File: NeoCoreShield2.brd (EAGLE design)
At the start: 70.9 x 70.4 mm, 41 parts, among them J6 BINDER_M12_PAR_8_DIP, J7 BINDER_M12_PAR_8_DIP, J8 BINDER_M12_PAR_8_DIP, J9 BINDER_M12_PAR_8_DIP, Q1 2.5A/30V/105mΩ, Q2 310mA/60V/1.6Ω, Q3 2.5A/30V/105mΩ, Q4 2.5A/30V/105mΩ, Q5 310mA/60V/1.6Ω, Q6 310mA/60V/1.6Ω

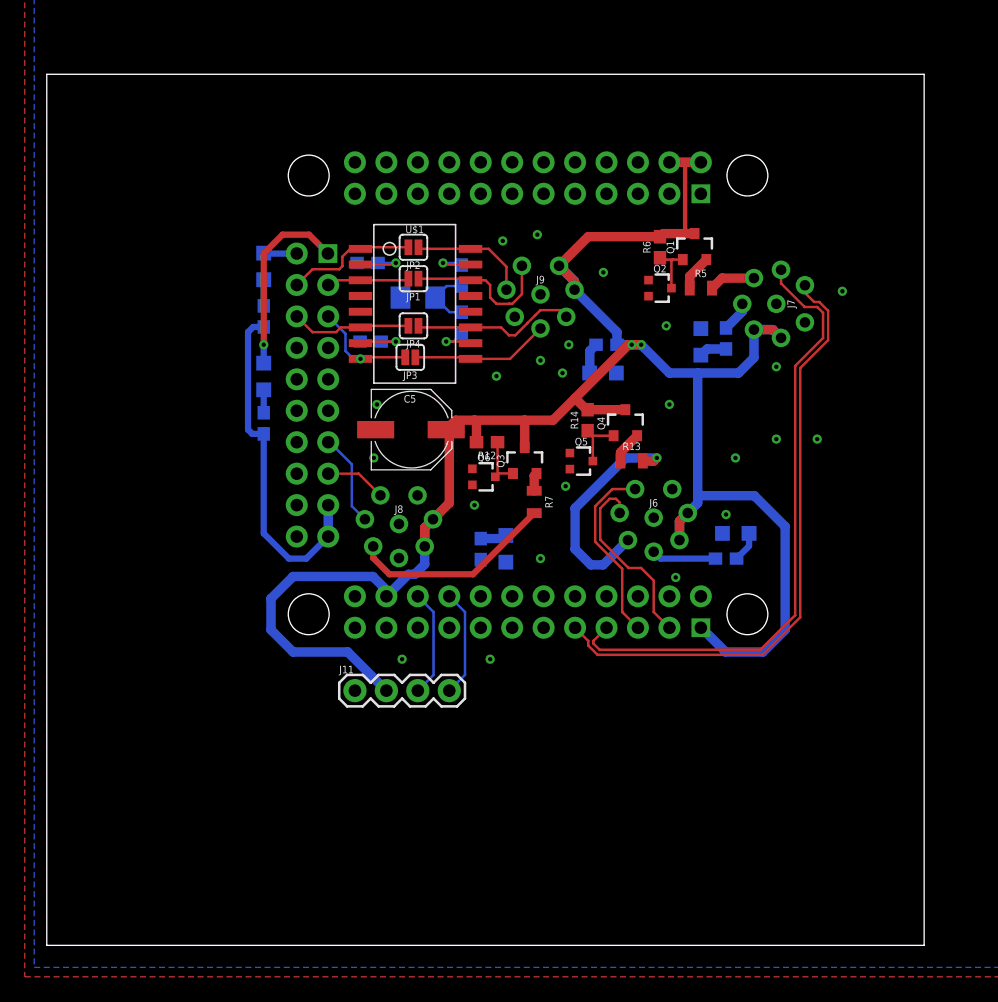
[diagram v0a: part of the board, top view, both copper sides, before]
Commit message: Routed Neo Core Shields
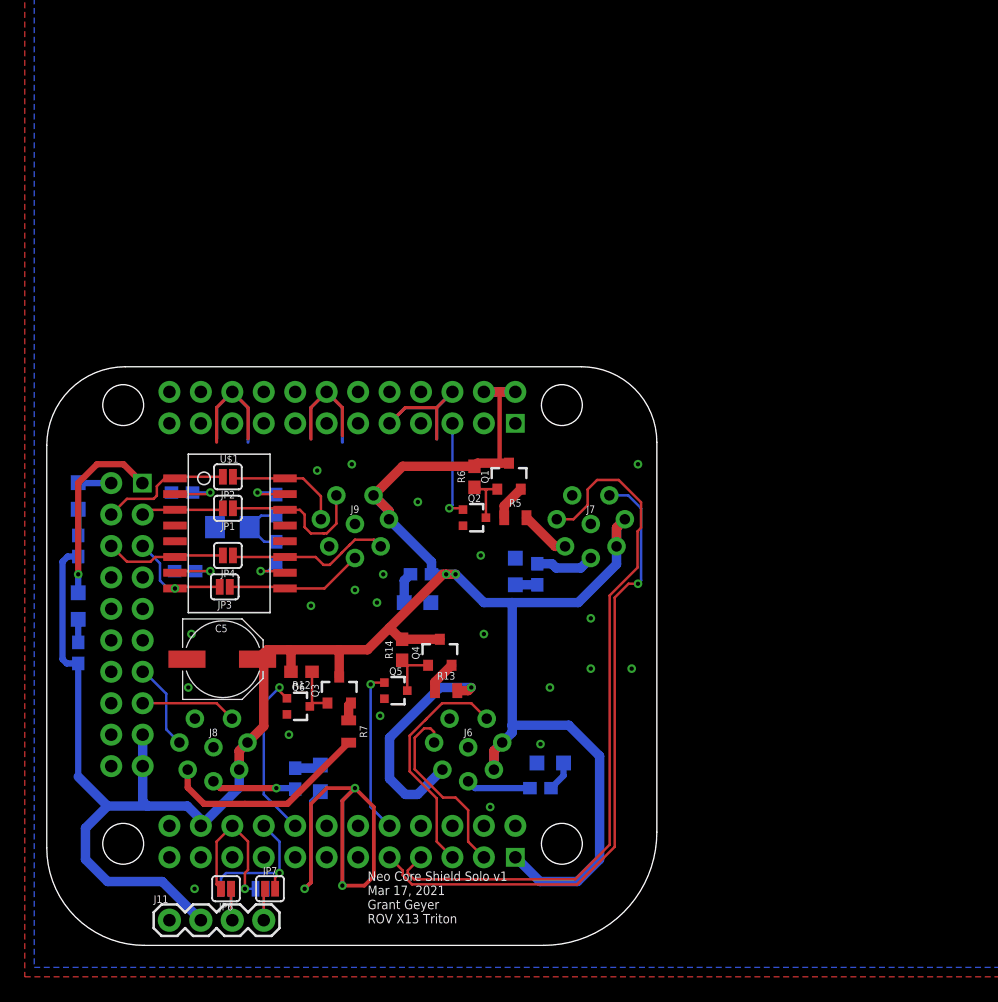
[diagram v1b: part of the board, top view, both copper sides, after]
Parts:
- added JP5, JP6, JP7, JP8: JUMPER-SMT_2_NO_SILK, SparkFun-Jumpers:SMT-JUMPER_2_NO_SILK
- moved R3 24.4 mm to (39.6, 30.0)
- moved C5 24.0 mm to (14.2, 23.1)
- moved D1 23.8 mm to (37.8, 30.2)
- moved Q2 23.8 mm to (34.5, 34.5)
- moved R10 23.8 mm to (30.2, 30.0)
- moved R5 23.8 mm to (37.8, 34.5)
- moved R6 23.8 mm to (34.5, 37.8)
- moved U1 23.8 mm to (37.8, 7.11)
- moved C1 23.8 mm to (11.2, 30.2)
- moved C2 23.8 mm to (10.9, 36.6)
- moved C3 23.8 mm to (15.0, 33.8)
- moved D2 23.8 mm to (22.1, 13.5)
- moved D3 23.8 mm to (2.54, 27.4)
- moved D5 23.8 mm to (30.0, 27.7)
- moved D6 23.8 mm to (40.6, 14.7)
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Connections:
- new net UART_RX_TX: J11.3, JP5.1, JP6.1
- new net UART_TX_RX: J11.4, JP7.1, JP8.1
- net GND: now also J6.2, J7.2, J8.2; no longer J6.1, J7.1, J8.1
- net LED_CONTROL1: now also U1.10
- net LED_CONTROL2: now also U1.49
- net UART_RX: now also JP5.2, JP7.2; no longer J11.4
- net UART_TX: now also JP6.2, JP8.2; no longer J11.3
- net USB_CAM_1_N: now also J6.1; no longer J6.2
- net USB_CAM_2_N: now also J7.1; no longer J7.2
- net USB_CAM_3_N: now also J8.1; no longer J8.2
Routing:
- net GND: track 0.00 -> 99.2 mm, vias 23 -> 24
- net LED_CONTROL3: track 0.00 -> 13.9 mm, vias 0 -> 1
- net LED_CONTROL1: track 0.00 -> 13.2 mm, vias 0 -> 1
- net LED_CONTROL2: track 0.00 -> 8.12 mm, vias 0 -> 1
- net USB_CAM_2_P: track 50.2 -> 57.7 mm
- net CONN_SENSE3: track 0.00 -> 6.87 mm, vias 0 -> 1
- net UART_TX_RX: track 0.00 -> 5.20 mm
- net UART_RX_TX: track 0.00 -> 5.16 mm
- net 5V: track 193.2 -> 198.2 mm
- net USB_CAM_1_N: track 15.0 -> 19.1 mm
- net UART_TX: track 8.67 -> 12.3 mm, vias 0 -> 1
- net USB_CAM_2_N: track 49.3 -> 52.2 mm, vias 0 -> 1
- net UART_RX: track 8.67 -> 11.5 mm, vias 0 -> 1
- net USB_CAM_3_N: track 4.94 -> 7.73 mm
- net CONN_SENSE2: track 2.49 -> 4.79 mm
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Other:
- board size 70.9 x 70.4 mm -> 49.3 x 46.7 mm
- board text added: "Neo Core Shield Solo v1 Mar 17, 2021 Grant Geyer ROV X13 Triton"

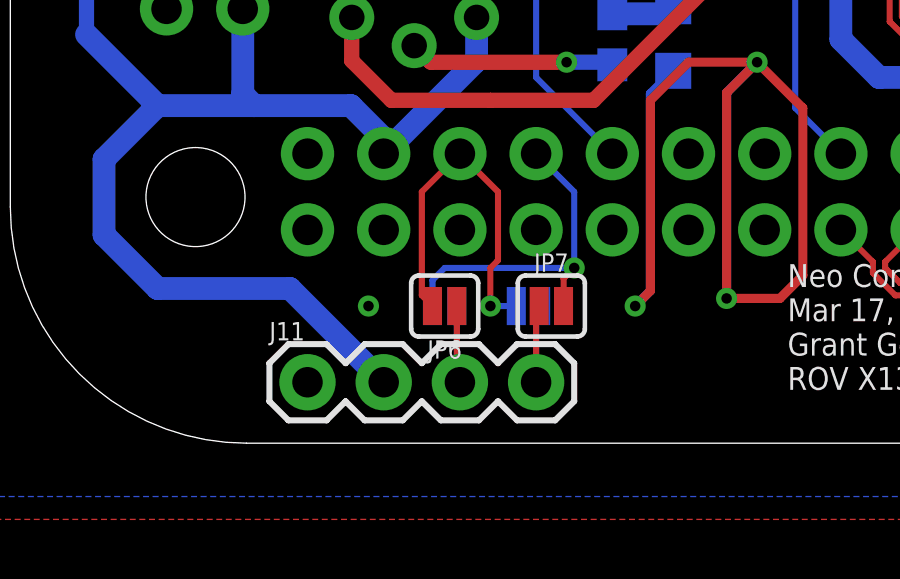
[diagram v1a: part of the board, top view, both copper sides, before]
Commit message: Neo Core Nano Pi Shield order
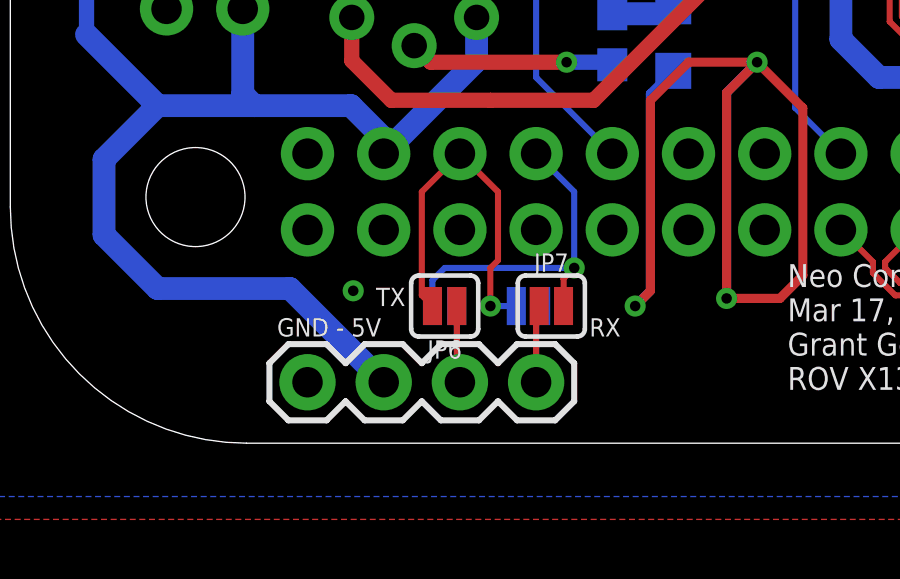
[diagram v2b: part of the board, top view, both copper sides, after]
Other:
- board text added: "GND - 5V"
- board text added: "RX"
- board text added: "TX"
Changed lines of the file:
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@@
 Grant Geyer
 ROV X13 Triton</text>
+<text x="12.192" y="4.572" size="0.6096" layer="25">TX</text>
+<text x="19.304" y="3.556" size="0.6096" layer="25">RX</text>
+<text x="8.89" y="3.556" size="0.6096" layer="25">GND - 5V</text>
 </plain>
 <attributes>
@@
 </element>
 <element name="J11" library="SparkFun-Connectors" library_urn="urn:adsk.eagle:library:513" package="1X04" package3d_urn="urn:adsk.eagle:package:38085/1" value="" x="9.906" y="2.032" smashed="yes">
-<attribute name="NAME" x="8.636" y="3.429" size="0.6096" layer="25" font="vector" ratio="20"/>
 <attribute name="PROD_ID" value="CONN-09696" x="9.906" y="2.032" size="1.778" layer="27" display="off"/>
 <attribute name="VALUE" x="8.636" y="0" size="0.6096" layer="27" font="vector" ratio="20"/>
@@
 <via x="21.336" y="27.432" extent="1-16" drill="0.35"/>
 <via x="21.844" y="38.354" extent="1-16" drill="0.35"/>
-<via x="11.938" y="4.572" extent="1-16" drill="0.35"/>
+<via x="11.43" y="5.08" extent="1-16" drill="0.35"/>
 <via x="20.828" y="4.572" extent="1-16" drill="0.35"/>
 <via x="24.892" y="12.7" extent="1-16" drill="0.35"/>
